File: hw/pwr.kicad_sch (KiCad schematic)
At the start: 15 parts, among them J1 Screw_Terminal_01x02, K1 Relay_DPDT, Q8 MMBT3904

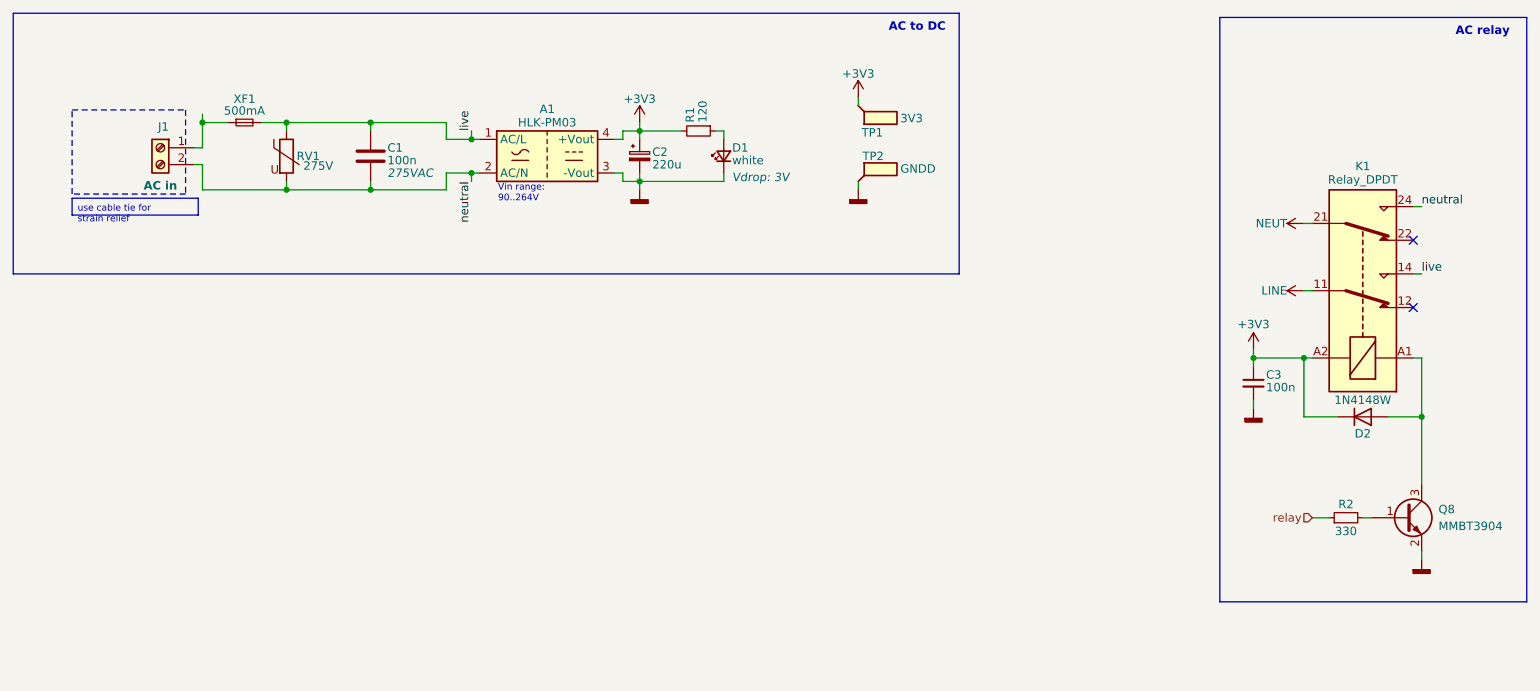
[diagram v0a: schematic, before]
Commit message: V2.0 (#2)
* **Hardware & Mechanical Design**
  * Updated design files and exports.
  * Split chassis and top plate into variants.
  * Changed enclosure folder structure.
  * Hid alignment/dimension layers; removed duplicate models.
  * Added mechanical parts and notes to schematics.

* **Firmware**
  * Updated firmware and added new versions.
  * Introduced firmware variants and consolidated them into packages.
  * Added common.yaml.
  * Moved effects out of packages.

* **Project Structure & Tooling**
  * Added BOM exports and fixed script permissions.
  * Updated and cleaned export folders.
  * Added ESPHome auto-generated `.gitignore`.
  * Fixed included libraries.
  * Miscellaneous corrections, reviews, merges, and cleanup commits.

* **Documentation & README**
  * Multiple revisions for clarity, formatting, structure, and consistency.
  * Added safety warnings for mains voltage operation.
  * Updated table of contents, badges, links, images, and repository structure sections.
  * Added roadmap, split release and change logs, reformatted release log.
  * Added links to schematic, PCB, BOMs, and iBOM.
  * Added additional documentation files.

* **Images, Photos & Media**
  * Updated, renamed, resized, and reformatted images.
  * Improved README image layout (width adjustments, centering, reduced size).
  * Added photos and screenshots across README and sub-readmes.
  * Added animations and animation exports; removed obsolete images.
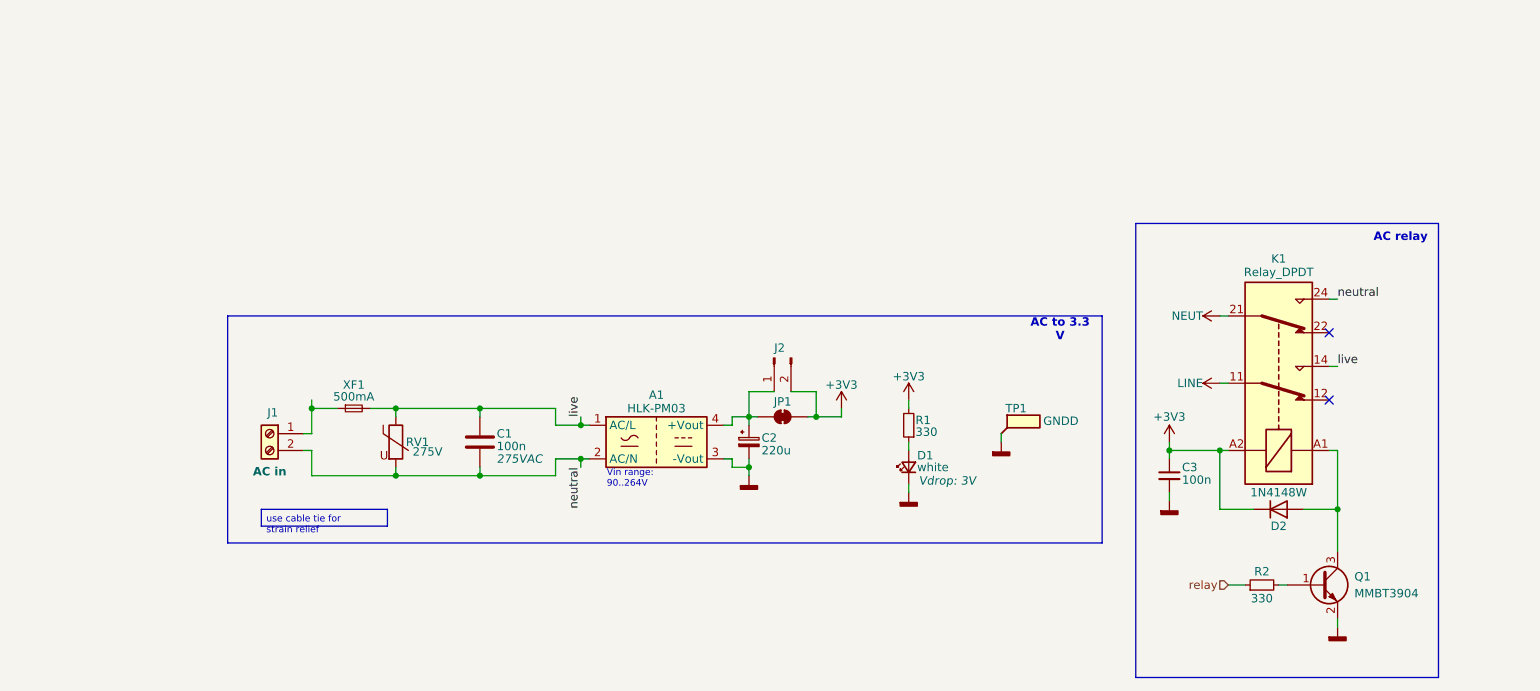
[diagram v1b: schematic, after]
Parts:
- removed TP1: 3V3, TestPoint:TestPoint_Pad_D1.0mm, symbol Connector:TestPoint_Flag
- added J2: Conn_01x02_Pin, Connector_PinSocket_2.54mm:PinSocket_1x02_P2.54mm_Vertical, symbol Connector:Conn_01x02_Pin
- added JP1: SolderJumper_2_Bridged, Jumper:SolderJumper-2_P1.3mm_Bridged_RoundedPad1.0x1.5mm, symbol Jumper:SolderJumper_2_Bridged
- R1: value 120 -> 330
- renumbered Q8 to Q1, TP2 to TP1
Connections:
- net +3V3: now also J2.2 (Pin_2), JP1.2 (B); no longer A1.4 (+Vout), C2.1
- new net: A1.4 (+Vout), C2.1, J2.1 (Pin_1), JP1.1 (A)
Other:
- title: LEDDs -> Power
- moved on the sheet: A1, C1, C2, C3, D1, D2, J1, K1, Q1, R1, R2, RV1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
